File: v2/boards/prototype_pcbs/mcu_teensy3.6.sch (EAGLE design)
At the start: 9 parts, among them Q1 BS108, U1 TEENSY3_6, U2 MCP101

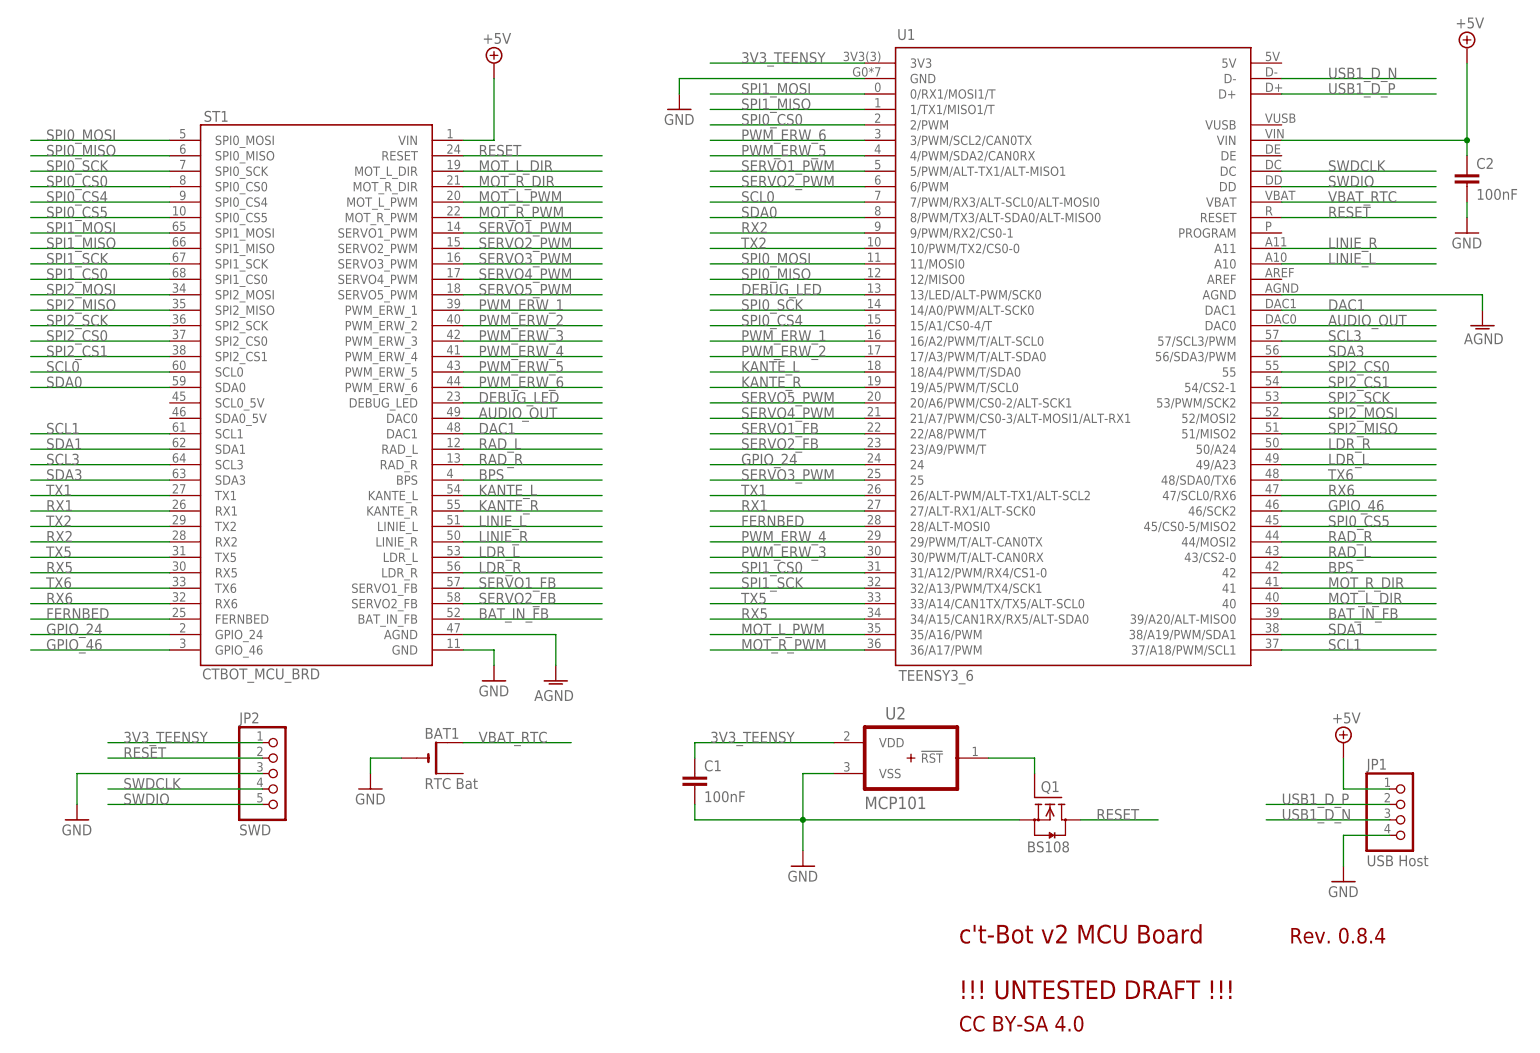
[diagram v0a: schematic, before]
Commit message: folder structure cleanup, 3d model: base updated
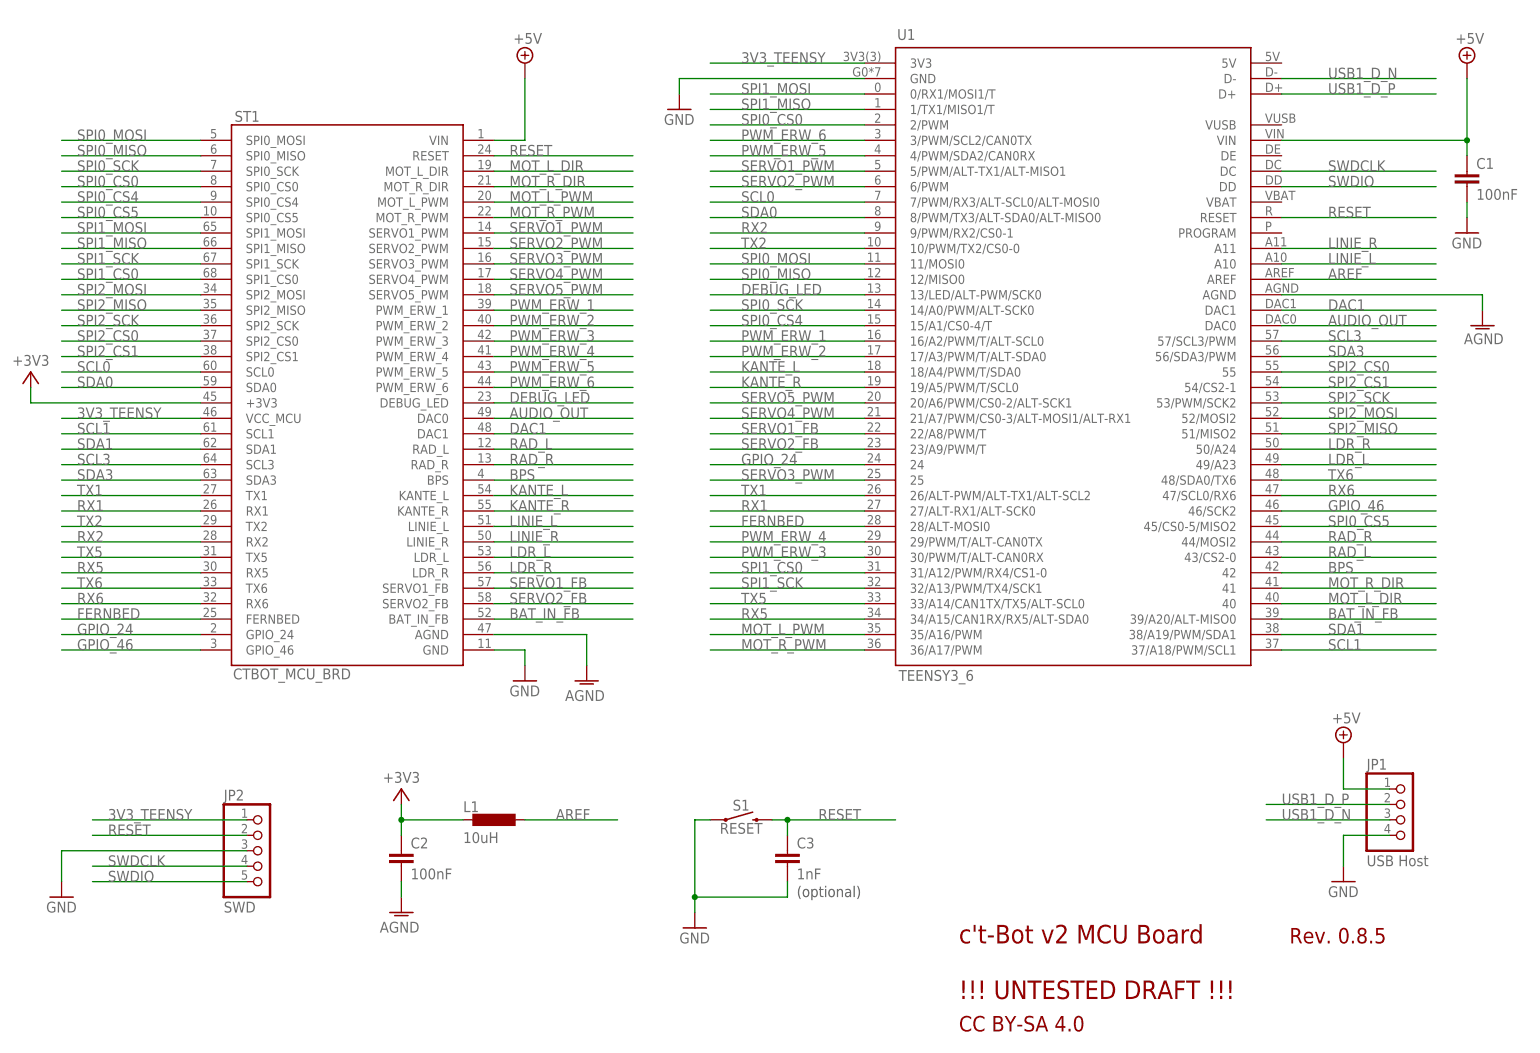
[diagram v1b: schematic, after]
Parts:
- removed BAT1: RTC Bat, adafruit:CR1220SMT
- removed Q1: BS108, ct-bot:BS108
- removed U2: MCP101, ct-bot:MCP101
- added C3: 1nF, rcl:C-EU025-025X050
- added L1: 10uH, rcl:L-EU0207/10
- added S1: RESET, SparkFun-Switches:MOMENTARY-SWITCH-SPST-PTH-6.0MM
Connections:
- removed net N$1: Q1.G, U2.!RST
- removed net VBAT_RTC: BAT1.+, U1.VBAT
- new net +3V3: C2.1, L1.2, ST1.+3V3
- new net AREF: L1.1, U1.AREF
- net +5V: now also C1.1; no longer C2.1
- net 3V3_TEENSY: now also ST1.VCC_MCU; no longer C1.1, U2.VDD
- net AGND: now also C2.2
- net GND: now also C3.2, S1.1; no longer BAT1.-, C2.2, Q1.S, U2.VSS
- net RESET: now also C3.1, S1.2; no longer Q1.D
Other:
- note added: "(optional)"
- note added: "Rev. 0.8.5"
- note removed: "Rev. 0.8.4"
- moved on the sheet: C1, C2, JP2, ST1
